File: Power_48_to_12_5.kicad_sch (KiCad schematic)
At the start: 6 parts

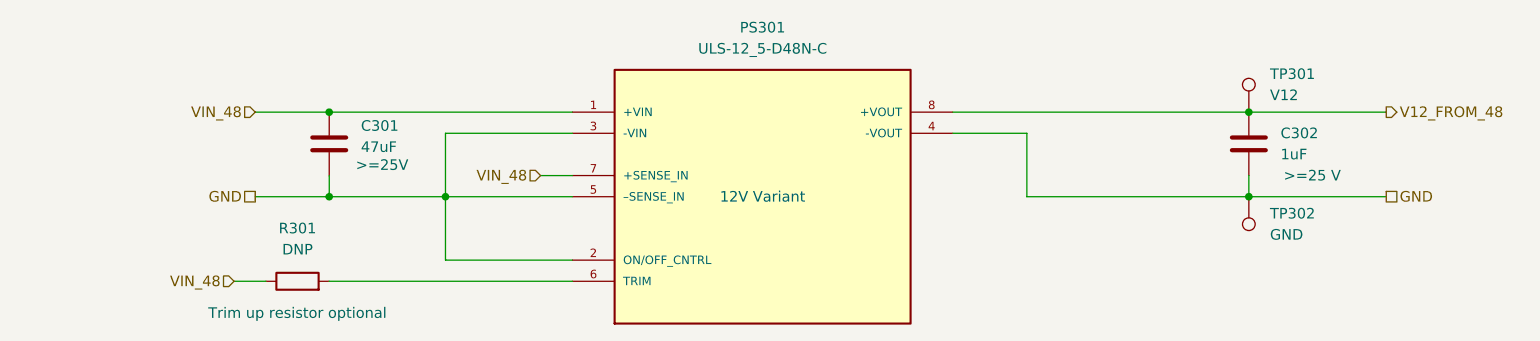
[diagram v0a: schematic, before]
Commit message: Update to fix power connection mistakes in both IWCD and HK configurations. For IWCD added bridge rectifier diodes needed for PoE, for HK updated to look at correct ref voltage for the 12V generation DC/DC, rotated the TVS to correct orientation and updated input diodes to be >=100V
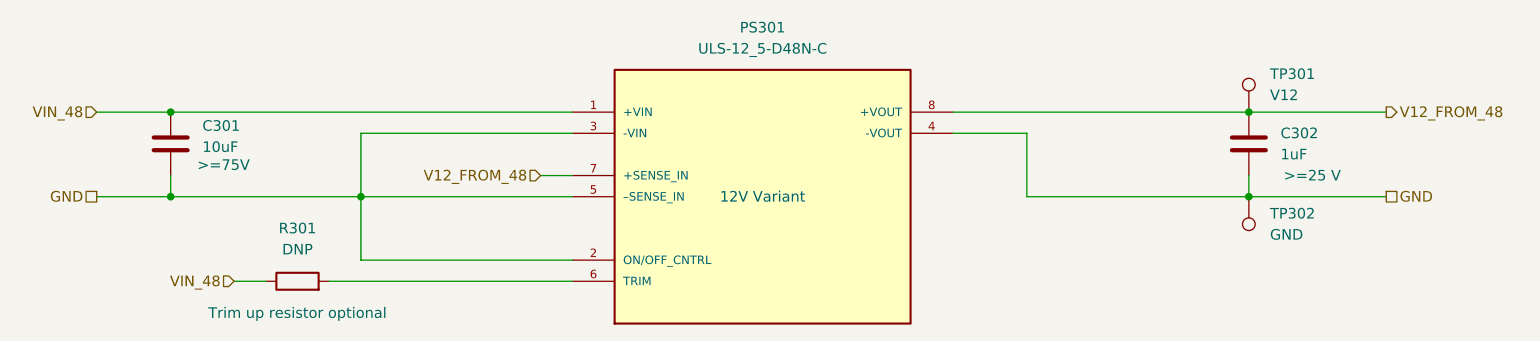
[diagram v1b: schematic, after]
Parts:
- C301: value 47uF -> 10uF; Purpose >=25V -> >=75V
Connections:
- net V12_FROM_48: now also PS301.7 (+SENSE_IN)
- net VIN_48: no longer PS301.7 (+SENSE_IN)
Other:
- moved on the sheet: C301
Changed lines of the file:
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@@
 	)
 	(junction
-		(at 110.49 91.44)
-		(diameter 0)
-		(color 0 0 0 0)
-	)
-	(junction
-		(at 96.52 81.28)
-		(diameter 0)
-		(color 0 0 0 0)
-	)
-	(junction
-		(at 96.52 91.44)
+		(at 77.47 81.28)
+		(diameter 0)
+		(color 0 0 0 0)
+	)
+	(junction
+		(at 77.47 91.44)
+		(diameter 0)
+		(color 0 0 0 0)
+	)
+	(junction
+		(at 100.33 91.44)
 		(diameter 0)
 		(color 0 0 0 0)
@@
 	(wire
 		(pts
-			(xy 110.49 91.44) (xy 125.73 91.44)
-		)
-		(stroke
-			(width 0)
-			(type default)
-		)
-	)
-	(wire
-		(pts
-			(xy 110.49 83.82) (xy 125.73 83.82)
+			(xy 100.33 83.82) (xy 125.73 83.82)
 		)
 		(stroke
@@
 	(wire
 		(pts
-			(xy 96.52 91.44) (xy 110.49 91.44)
-		)
-		(stroke
-			(width 0)
-			(type default)
-		)
-	)
-	(wire
-		(pts
-			(xy 110.49 83.82) (xy 110.49 91.44)
+			(xy 77.47 91.44) (xy 100.33 91.44)
+		)
+		(stroke
+			(width 0)
+			(type default)
+		)
+	)
+	(wire
+		(pts
+			(xy 100.33 83.82) (xy 100.33 91.44)
 		)
 		(stroke
@@
 	(wire
 		(pts
-			(xy 87.63 91.44) (xy 96.52 91.44)
-		)
-		(stroke
-			(width 0)
-			(type default)
-		)
-	)
-	(wire
-		(pts
-			(xy 87.63 81.28) (xy 96.52 81.28)
-		)
-		(stroke
-			(width 0)
-			(type default)
-		)
-	)
-	(wire
-		(pts
-			(xy 96.52 81.28) (xy 125.73 81.28)
+			(xy 68.58 91.44) (xy 77.47 91.44)
+		)
+		(stroke
+			(width 0)
+			(type default)
+		)
+	)
+	(wire
+		(pts
+			(xy 68.58 81.28) (xy 77.47 81.28)
+		)
+		(stroke
+			(width 0)
+			(type default)
+		)
+	)
+	(wire
+		(pts
+			(xy 77.47 81.28) (xy 125.73 81.28)
 		)
 		(stroke
@@
 	(wire
 		(pts
-			(xy 110.49 99.06) (xy 125.73 99.06)
-		)
-		(stroke
-			(width 0)
-			(type default)
-		)
-	)
-	(wire
-		(pts
-			(xy 110.49 91.44) (xy 110.49 99.06)
+			(xy 100.33 99.06) (xy 125.73 99.06)
+		)
+		(stroke
+			(width 0)
+			(type default)
+		)
+	)
+	(wire
+		(pts
+			(xy 100.33 91.44) (xy 100.33 99.06)
 		)
 		(stroke
@@
 	(wire
 		(pts
-			(xy 96.52 88.9) (xy 96.52 91.44)
+			(xy 77.47 88.9) (xy 77.47 91.44)
 		)
 		(stroke
@@
 		(pts
 			(xy 121.92 88.9) (xy 125.73 88.9)
+		)
+		(stroke
+			(width 0)
+			(type default)
+		)
+	)
+	(wire
+		(pts
+			(xy 100.33 91.44) (xy 125.73 91.44)
 		)
 		(stroke
@@
 		)
 	)
-	(hierarchical_label "VIN_48"
+	(hierarchical_label "V12_FROM_48"
 		(shape input)
 		(at 121.92 88.9 180)
@@
 	(hierarchical_label "GND"
 		(shape passive)
-		(at 87.63 91.44 180)
+		(at 68.58 91.44 180)
 		(effects
 			(font
@@
 	(hierarchical_label "VIN_48"
 		(shape input)
-		(at 87.63 81.28 180)
+		(at 68.58 81.28 180)
 		(effects
 			(font
@@
 	(symbol
 		(lib_id "Device:C")
-		(at 96.52 85.09 0)
+		(at 77.47 85.09 0)
 		(unit 1)
 		(exclude_from_sim no)
@@
 		(dnp no)
 		(property "Reference" "C301"
-			(at 100.33 82.9309 0)
+			(at 81.28 82.9309 0)
 			(effects
 				(font
@@
 			)
 		)
-		(property "Value" "47uF"
-			(at 100.33 85.4709 0)
+		(property "Value" "10uF"
+			(at 81.28 85.4709 0)
 			(effects
 				(font
@@
 		)
 		(property "Footprint" "Capacitor_SMD:CP_Elec_6.3x5.4"
-			(at 97.4852 88.9 0)
+			(at 78.4352 88.9 0)
 			(effects
 				(font
@@
 		)
 		(property "Datasheet" "~"
-			(at 96.52 85.09 0)
-			(effects
-				(font
-					(size 1.27 1.27)
-				)
-				(hide yes)
-			)
-		)
-		(property "Description" "Unpolarized capacitor"
-			(at 96.52 85.09 0)
-			(effects
-				(font
-					(size 1.27 1.27)
-				)
-				(hide yes)
-			)
-		)
-		(property "Purpose" ">=25V"
-			(at 102.87 87.63 0)
-			(effects
-				(font
+			(at 77.47 85.09 0)
+			(effects
+				(font
+					(size 1.27 1.27)
+				)
+				(hide yes)
+			)
+		)
+		(property "Description" "Unpolarized capacitor,  Wurth 865060845002"
+			(at 77.47 85.09 0)
+			(effects
+				(font
+					(size 1.27 1.27)
+				)
+				(hide yes)
+			)
+		)
+		(property "Purpose" ">=75V"
+			(at 83.82 87.63 0)
+			(effects
+				(font
